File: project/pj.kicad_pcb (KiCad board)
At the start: 2 copper layers, 65 x 56.5 mm, 21 parts, among them J1 RPi_GPIO, J10 Pi PWR enable, J11 Conn_01x03_Pin, J2 2B+, J3 zero, J4 3A+, J5 3B+, J6 Pi 4, J7 Reset Pico, J8 Reset Pi, J9 Pi External PWR, SW1 Reset Pi, SW2 Reset Pico, U1 W25Q32JVSS

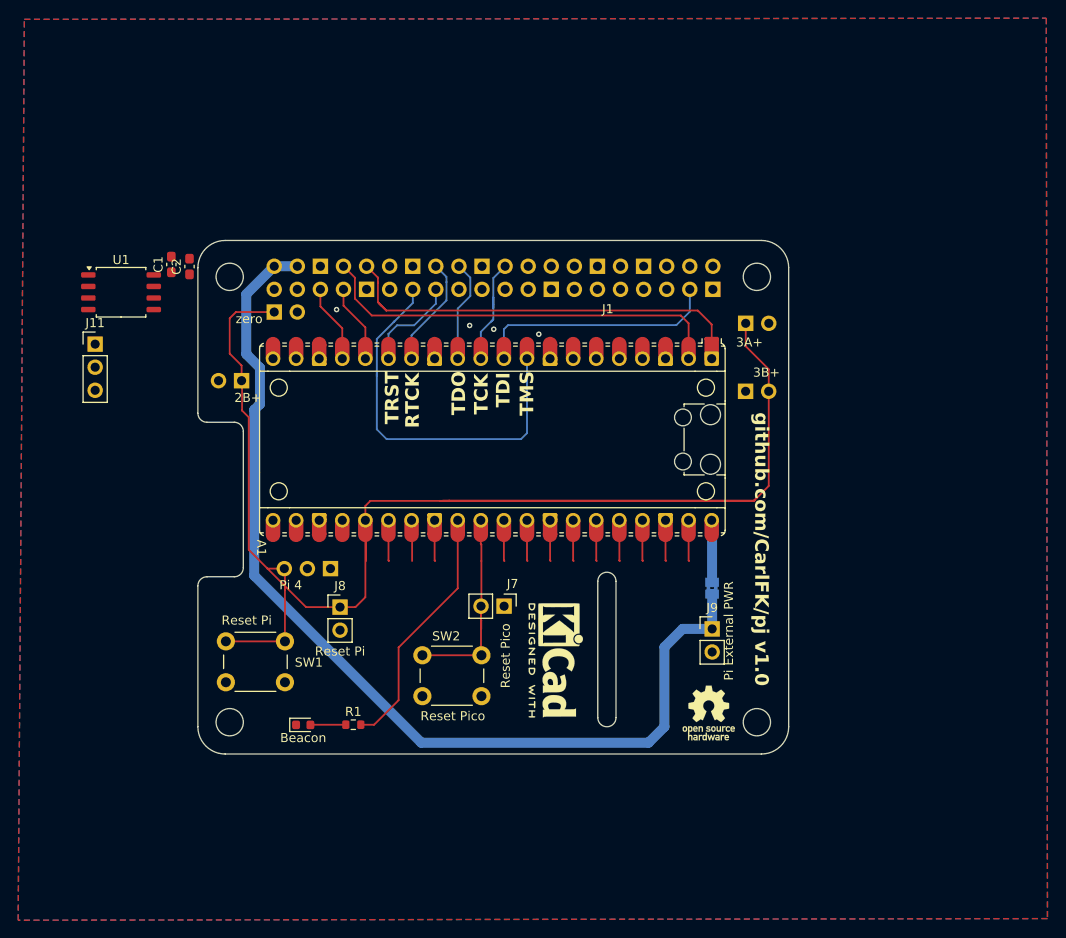
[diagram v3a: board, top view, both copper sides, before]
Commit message: added spi, moved zero run
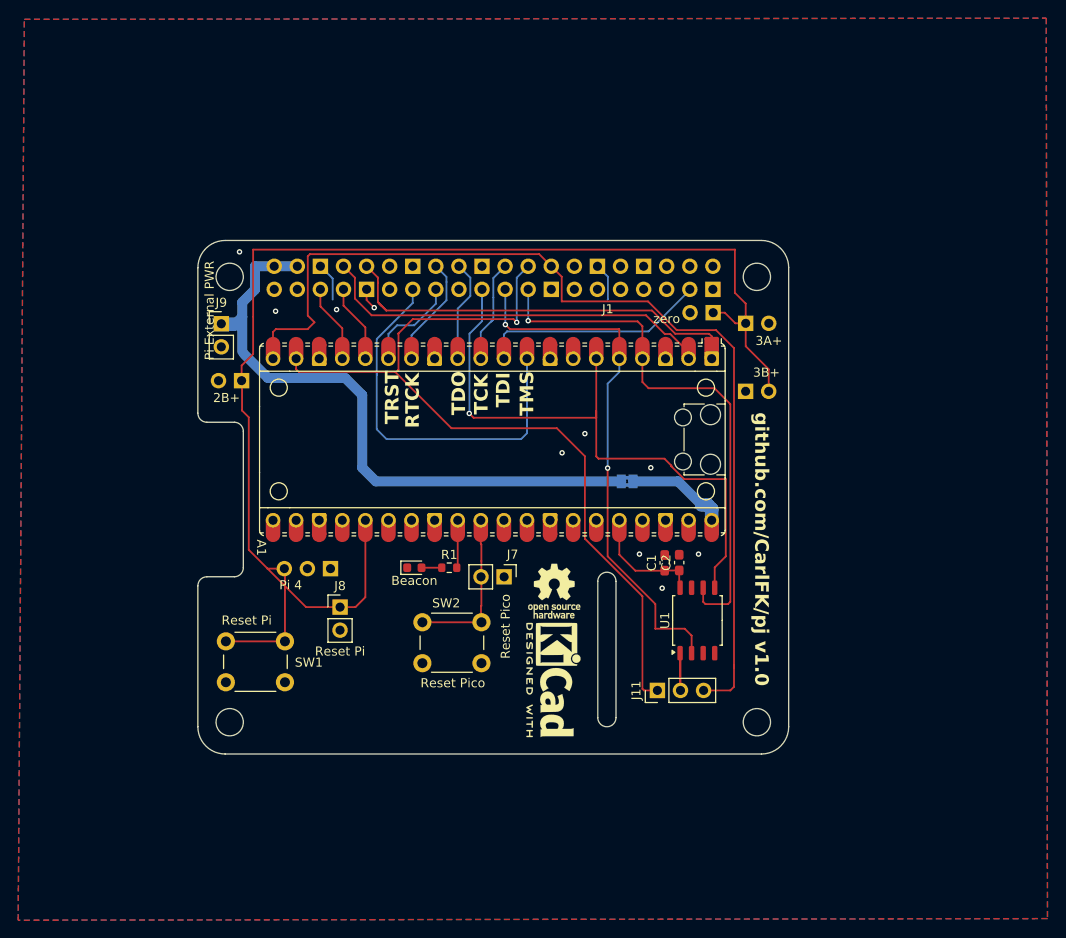
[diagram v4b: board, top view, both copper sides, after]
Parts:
- moved U1 73.0 mm to (91.4, 82.3), turned to 90 degrees
- moved J11 72.6 mm to (87.0, 90.0), turned to 90 degrees
- moved J9 63.6 mm to (39.0, 49.7)
- moved C1 63.4 mm to (87.8, 76.0)
- moved C2 63.0 mm to (89.4, 75.9)
- moved J3 48.3 mm to (93.1, 48.4), turned to 90 degrees
- moved REF** 21.6 mm to (75.6, 79.1)
- moved D1 21.2 mm to (60.2, 76.5)
- moved R1 20.2 mm to (64.1, 76.5)
- moved J10 15.0 mm to (83.7, 67.0), turned to 180 degrees
- moved SW2 3.63 mm to (67.6, 87.0)
- moved J7 3.23 mm to (70.1, 77.5)
- moved REF** 2.18 mm to (75.5, 88.8)
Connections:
- A1 pad 29: Net-(A1-GPIO22) -> GND
- D1 pad 2: Net-(D1-A) -> GND
- R1 pad 1: Net-(D1-A) -> GND
- R1 pad 2: Net-(A1-GPIO22) -> GND
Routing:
- net /RPI_SPI_CE1: track 0.00 -> 109.4 mm
- net /RPI_SPI_CE0: track 0.00 -> 91.8 mm, vias 0 -> 1
- net /RPI_SPI_MOSI: track 0.19 -> 67.7 mm, vias 0 -> 1
- net /RPI_SPI_CLK: track 0.00 -> 59.6 mm, vias 0 -> 1
- net /RPI_SPI_MISO: track 0.19 -> 58.5 mm, vias 0 -> 2
- net Net-(J10-Pin_2): track 110.9 -> 69.2 mm
- net /reset pi: track 177.9 -> 148.7 mm
- net Net-(A1-GPIO22): track 27.8 -> 0.00 mm
- net GND: track 9.20 -> 18.3 mm, vias 4 -> 10
- net +3.3V: track 4.51 -> 13.0 mm
- net Net-(J11-Pin_2): track 0.00 -> 7.64 mm
- net Net-(A1-RUN): track 25.0 -> 19.5 mm
- net unconnected-(A1-GPIO20-Pad26): track 4.52 -> 0.00 mm
- net unconnected-(A1-VSYS-Pad39): track 4.51 -> 0.00 mm
- net unconnected-(A1-GPIO28_ADC2-Pad34): track 4.51 -> 0.00 mm
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
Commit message: done with spi
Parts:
- added R2: 10k, Resistor_SMD:R_0603_1608Metric, F.Cu at (43.3, 48.2)
- moved SW1 6.15 mm to (44.2, 80.7), turned to -90 degrees
- moved D1 1.95 mm to (62.1, 76.1), turned to 90 degrees
- moved R1 0.89 mm to (64.9, 76.2), turned to 90 degrees
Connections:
- net +3.3V renamed /pico3v3
- J1 pad 1: unconnected-(J1-3.3V-Pad1) -> Net-(J1-3.3V-Pad1)
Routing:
- net GND: track 18.3 -> 10.7 mm, vias 10 -> 12
- net /reset pi: track 148.7 -> 145.1 mm
- net Net-(J1-3.3V-Pad1): track 0.00 -> 2.97 mm
- net /RPI_SPI_CE1: track 109.4 -> 107.3 mm

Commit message: v2.0
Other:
- board text added: "github.com/CarlFK/pj v2.0"
- board text removed: "github.com/CarlFK/pj v1.0"
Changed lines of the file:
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@@
 		(fp_arc
 			(start 10.579676 25.189937)
-			(mid 10.357946 25.493957)
+			(mid 10.357958 25.493991)
 			(end 10 25.61)
 			(stroke
@@
 		(tags "resistor")
 		(property "Reference" "R2"
-			(at 0 -1.43 360)
+			(at 0 -1.43 0)
 			(layer "F.SilkS")
 			(effects
@@
 		)
 		(property "Value" "10k"
-			(at 0 1.43 360)
+			(at 0 1.43 0)
 			(layer "F.Fab")
 			(effects
@@
 		)
 		(fp_text user "${REFERENCE}"
-			(at 0 0 360)
+			(at 0 0 0)
 			(layer "F.Fab")
 			(effects
@@
 		)
 	)
-	(gr_text "github.com/CarlFK/pj v1.0"
+	(gr_text "github.com/CarlFK/pj v2.0"
 		(at 97.55 59.4 270)
 		(layer "F.SilkS")

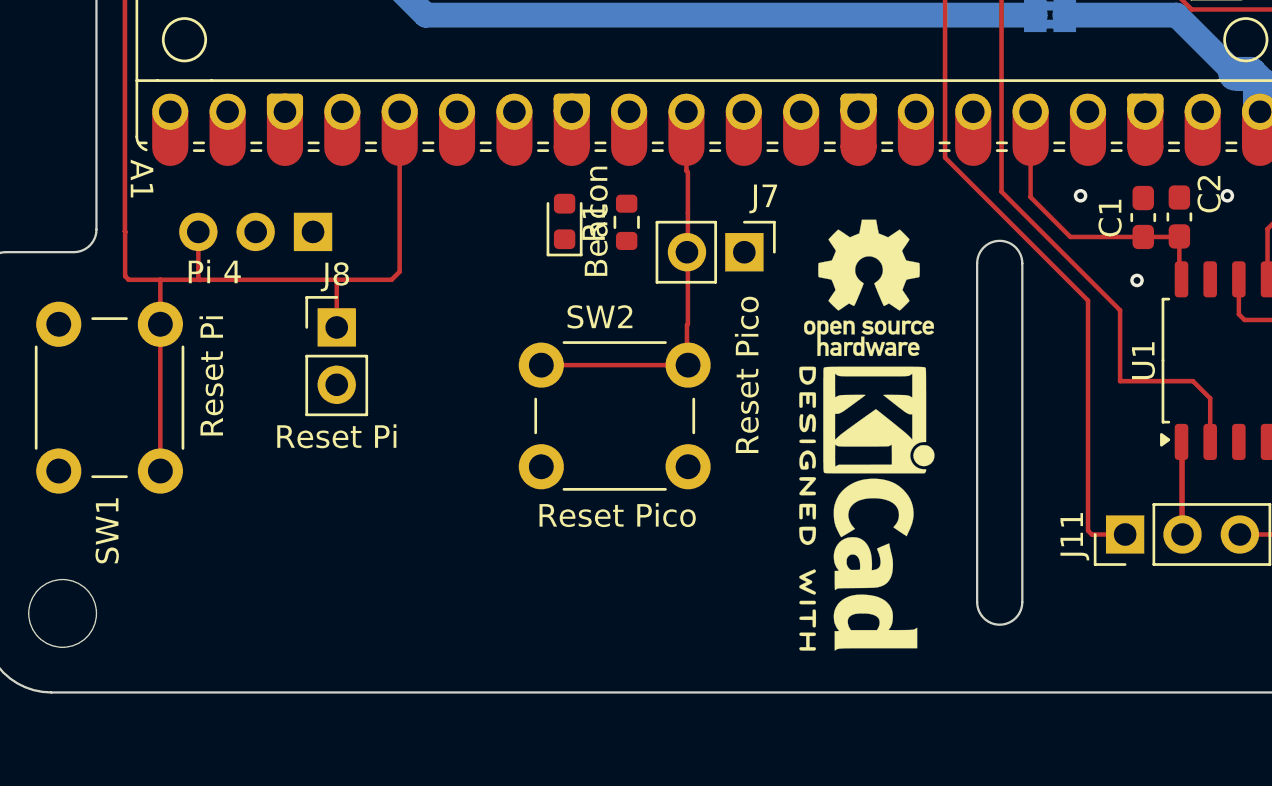
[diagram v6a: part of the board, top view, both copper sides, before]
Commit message: move OH logo, remove some extra vias
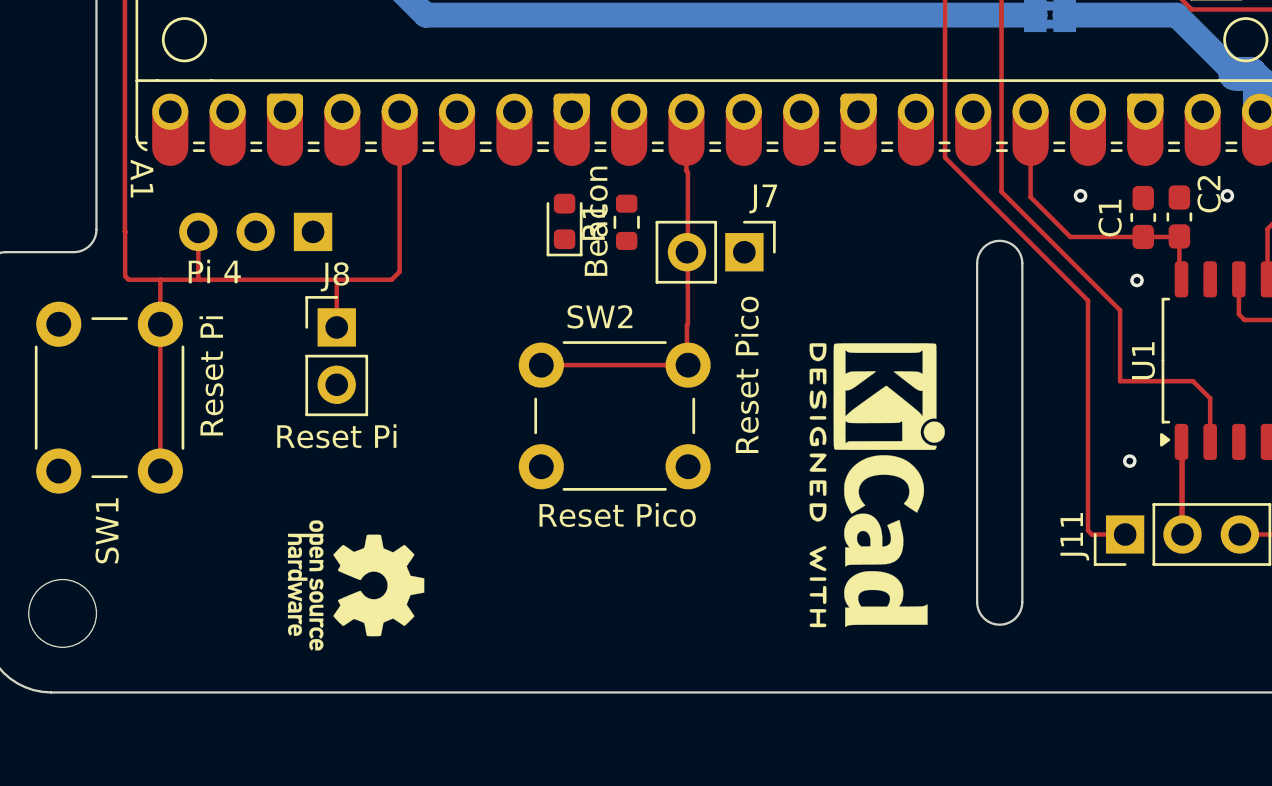
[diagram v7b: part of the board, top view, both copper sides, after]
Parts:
- moved REF** 26.3 mm to (52.9, 92.2), turned to -90 degrees
- moved REF** 1.14 mm to (76.0, 87.8)
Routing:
- net GND: vias 12 -> 13
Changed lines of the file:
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@@
 		(fp_arc
 			(start 10.579676 25.189937)
-			(mid 10.357958 25.493991)
+			(mid 10.35796 25.493961)
 			(end 10 25.61)
 			(stroke
@@
 	(footprint "Symbol:KiCad-Logo2_5mm_SilkScreen"
 		(layer "F.Cu")
-		(at 75.55 88.85 -90)
+		(at 76.01 87.81 -90)
 		(descr "KiCad Logo")
 		(tags "Logo KiCad")
@@
 	(footprint "Symbol:OSHW-Logo_5.7x6mm_SilkScreen"
 		(layer "F.Cu")
-		(at 75.625 79.075)
+		(at 52.92 92.25 -90)
 		(descr "Open Source Hardware Logo")
 		(tags "Logo OSHW")
 		(property "Reference" "REF**"
-			(at 0 0 0)
+			(at 0 0 90)
 			(layer "F.SilkS")
 			(hide yes)
@@
 		)
 		(property "Value" "OSHW-Logo_5.7x6mm_SilkScreen"
-			(at 0.75 0 0)
+			(at 0.75 0 90)
 			(layer "F.Fab")
 			(hide yes)
@@
 		)
 		(property "Footprint" "Symbol:OSHW-Logo_5.7x6mm_SilkScreen"
-			(at 0 0 0)
+			(at 0 0 -90)
 			(unlocked yes)
 			(layer "F.SilkS")
@@
 		)
 		(property "Datasheet" ""
-			(at 0 0 0)
+			(at 0 0 -90)
 			(unlocked yes)
 			(layer "F.Fab")
@@
 		)
 		(property "Description" ""
-			(at 0 0 0)
+			(at 0 0 -90)
 			(unlocked yes)
 			(layer "F.Fab")
@@
 		(fp_poly
 			(pts
-				(xy -2.538261 1.465148) (xy -2.472479 1.494231) (xy -2.42254 1.542793) (xy -2.388374 1.610908) (xy -2.369907 1.698651)
-				(xy -2.368583 1.712351) (xy -2.367546 1.808939) (xy -2.380993 1.893602) (xy -2.408108 1.962221)
-				(xy -2.422627 1.984294) (xy -2.473201 2.031011) (xy -2.537609 2.061268) (xy -2.609666 2.073824)
-				(xy -2.683185 2.067439) (xy -2.739072 2.047772) (xy -2.787132 2.014629) (xy -2.826412 1.971175)
-				(xy -2.827092 1.970158) (xy -2.843044 1.943338) (xy -2.85341 1.916368) (xy -2.859688 1.882332) (xy -2.863373 1.83431)
-				(xy -2.864997 1.794931) (xy -2.865672 1.759219) (xy -2.739955 1.759219) (xy -2.738726 1.79477) (xy -2.734266 1.842094)
-				(xy -2.726397 1.872465) (xy -2.712207 1.894072) (xy -2.698917 1.906694) (xy -2.651802 1.933122)
-				(xy -2.602505 1.936653) (xy -2.556593 1.917639) (xy -2.533638 1.896331) (xy -2.517096 1.874859)
-				(xy -2.507421 1.854313) (xy -2.503174 1.827574) (xy -2.50292 1.787523) (xy -2.504228 1.750638) (xy -2.507043 1.697947)
-				(xy -2.511505 1.663772) (xy -2.519548 1.64148) (xy -2.533103 1.624442) (xy -2.543845 1.614703) (xy -2.588777 1.589123)
-				(xy -2.637249 1.587847) (xy -2.677894 1.602999) (xy -2.712567 1.634642) (xy -2.733224 1.68662) (xy -2.739955 1.759219)
-				(xy -2.865672 1.759219) (xy -2.866479 1.716621) (xy -2.863948 1.658056) (xy -2.856362 1.614007)
-				(xy -2.842681 1.579248) (xy -2.821865 1.548551) (xy -2.814147 1.539436) (xy -2.765889 1.494021)
-				(xy -2.714128 1.467493) (xy -2.650828 1.456379) (xy -2.619961 1.455471) (xy -2.538261 1.465148)
-			)
-			(stroke
-				(width 0.01)
-				(type solid)
-			)
-			(fill solid)
-			(layer "F.SilkS")
-		)
-		(fp_poly
-			(pts
 				(xy -0.201188 3.017822) (xy -0.270346 3.017822) (xy -0.310488 3.016645) (xy -0.331394 3.011772)
 				(xy -0.338922 3.001186) (xy -0.339505 2.994029) (xy -0.340774 2.979676) (xy -0.348779 2.976923)
@@
 		(fp_poly
 			(pts
+				(xy -2.538261 1.465148) (xy -2.472479 1.494231) (xy -2.42254 1.542793) (xy -2.388374 1.610908) (xy -2.369907 1.698651)
+				(xy -2.368583 1.712351) (xy -2.367546 1.808939) (xy -2.380993 1.893602) (xy -2.408108 1.962221)
+				(xy -2.422627 1.984294) (xy -2.473201 2.031011) (xy -2.537609 2.061268) (xy -2.609666 2.073824)
+				(xy -2.683185 2.067439) (xy -2.739072 2.047772) (xy -2.787132 2.014629) (xy -2.826412 1.971175)
+				(xy -2.827092 1.970158) (xy -2.843044 1.943338) (xy -2.85341 1.916368) (xy -2.859688 1.882332) (xy -2.863373 1.83431)
+				(xy -2.864997 1.794931) (xy -2.865672 1.759219) (xy -2.739955 1.759219) (xy -2.738726 1.79477) (xy -2.734266 1.842094)
+				(xy -2.726397 1.872465) (xy -2.712207 1.894072) (xy -2.698917 1.906694) (xy -2.651802 1.933122)
+				(xy -2.602505 1.936653) (xy -2.556593 1.917639) (xy -2.533638 1.896331) (xy -2.517096 1.874859)
+				(xy -2.507421 1.854313) (xy -2.503174 1.827574) (xy -2.50292 1.787523) (xy -2.504228 1.750638) (xy -2.507043 1.697947)
+				(xy -2.511505 1.663772) (xy -2.519548 1.64148) (xy -2.533103 1.624442) (xy -2.543845 1.614703) (xy -2.588777 1.589123)
+				(xy -2.637249 1.587847) (xy -2.677894 1.602999) (xy -2.712567 1.634642) (xy -2.733224 1.68662) (xy -2.739955 1.759219)
+				(xy -2.865672 1.759219) (xy -2.866479 1.716621) (xy -2.863948 1.658056) (xy -2.856362 1.614007)
+				(xy -2.842681 1.579248) (xy -2.821865 1.548551) (xy -2.814147 1.539436) (xy -2.765889 1.494021)
+				(xy -2.714128 1.467493) (xy -2.650828 1.456379) (xy -2.619961 1.455471) (xy -2.538261 1.465148)
+			)
+			(stroke
+				(width 0.01)
+				(type solid)
+			)
+			(fill solid)
+			(layer "F.SilkS")
+		)
+		(fp_poly
+			(pts
 				(xy 2.677898 1.456457) (xy 2.710096 1.464279) (xy 2.771825 1.492921) (xy 2.82461 1.536667) (xy 2.861141 1.589117)
 				(xy 2.86616 1.600893) (xy 2.873045 1.63174) (xy 2.877864 1.677371) (xy 2.879505 1.723492) (xy 2.879505 1.810693)
@@
 		(size 0.6)
 		(drill 0.3)
+		(layers "F.Cu" "B.Cu")
+		(free yes)
+		(net 7)
+	)
+	(via
+		(at 87.18 86.75)
+		(size 0.6)
+		(drill 0.3)
